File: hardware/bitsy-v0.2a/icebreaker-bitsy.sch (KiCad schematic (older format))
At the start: 94 parts, among them J1 Conn_01x01, J10 Conn_01x01, J11 Conn_01x01, J12 Conn_01x01, J13 Conn_01x01, J14 Jumper, J15 Jumper, J16 Jumper, J17 Jumper, J18 Jumper, J19 Jumper, J2 Conn_01x01, J20 Conn_01x01, J21 Conn_01x01, J22 Conn_01x01, J23 Conn_01x01, J24 Conn_01x01, J25 Conn_01x01, J26 Conn_01x01, J27 Conn_01x01, J28 Conn_01x01, J29 Conn_01x01, J3 Conn_01x01, J30 Conn_01x01, J31 Conn_01x01, J32 Conn_01x01, J33 Conn_01x01, J34 Conn_01x01, J35 Conn_01x01, J36 Conn_01x01, J37 Conn_01x01, J38 Jumper, J4 Conn_01x01, J41 Conn_01x01, J42 Conn_01x01, J43 Conn_01x01, J44 Conn_01x01, J45 Conn_01x01, J46 Conn_01x01, J47 Conn_01x01, J48 Conn_01x01, J49 Conn_01x01, J5 Conn_01x01, J6 Conn_01x01, J7 Conn_01x01, J8 Conn_01x01, J9 Conn_01x01, P1 USB_OTG, SW1 TACT, U1 USBLC6-2, U2 3.3V, U3 1V2, U5 W25Q, U6 ICE5LP4K-SG48, X1 12MHz

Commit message: Fixed #6 Oscillator pinout and schematic symbol.
Both bitsy and icebreaker.
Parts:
- X1: symbol pkl_device:Oscillator -> pkl_device:pkl_oscillator_sit2001
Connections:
- wire segments 315 -> 311
- no-connect marks 1 -> 2
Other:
- moved on the sheet: C4, R7
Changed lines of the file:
@@
 Title "iCEBreaker-bitsy"
 Date ""
-Rev "V0.2a"
+Rev "V0.1a"
 Comp "1BitSquared"
 Comment1 "2018 (C) 1BitSquared <info@1bitsquared.com>"
@@
 $EndComp
 $Comp
-L pkl_device:Oscillator X1
+L pkl_device:pkl_oscillator_sit2001 X1
 U 1 1 5A523EA3
-P 1550 3150
-F 0 "X1" H 1550 2755 60  0000 C CNN
-F 1 "12MHz" H 1550 2865 60  0000 C CNN
-F 2 "pkl_housings_sot:SOT-23-5" H 1550 3150 60  0001 C CNN
-F 3 "https://www.sitime.com/datasheet/SiT2001" H 1550 3150 60  0001 C CNN
-F 4 "12MHz Oscillator" H 1550 3150 50  0001 C CNN "Description"
-F 5 "SiTIME" H 1550 3150 50  0001 C CNN "Manufacturer"
-F 6 "SIT2001BI-S2-33E-12.000000G" H 1550 3150 50  0001 C CNN "MFN"
-F 7 "ANY" H 1550 3150 50  0001 C CNN "Source"
-F 8 "xtal-sot23-5-12mhz-osc" H -350 -3600 50  0001 C CNN "Key"
-	1    1550 3150
-	-1   0    0    1
+P 1750 3250
+F 0 "X1" H 1750 3600 60  0000 C CNN
+F 1 "12MHz" H 1750 3500 60  0000 C CNN
+F 2 "pkl_housings_sot:SOT-23-5" H 1750 3250 60  0001 C CNN
+F 3 "https://www.sitime.com/datasheet/SiT2001" H 1750 3250 60  0001 C CNN
+F 4 "xtal-sot23-5-12mhz-osc" H -150 -3500 50  0001 C CNN "Key"
+F 5 "12MHz Oscillator" H 1750 3250 50  0001 C CNN "Description"
+F 6 "SiTIME" H 1750 3250 50  0001 C CNN "Manufacturer"
+F 7 "SIT2001BI-S2-33E-12.000000G" H 1750 3250 50  0001 C CNN "MFN"
+F 8 "ANY" H 1750 3250 50  0001 C CNN "Source"
+	1    1750 3250
+	-1   0    0    -1
 $EndComp
 $Comp
 L pkl_device:pkl_R_Small R7
 U 1 1 5A52417F
-P 2150 3150
-F 0 "R7" V 2200 3300 50  0000 C CNN
-F 1 "10k" V 2200 3000 50  0000 C CNN
-F 2 "pkl_dipol:R_0402" H 2209 3057 60  0001 L CNN
-F 3 "" H 2150 3150 60  0000 C CNN
-F 4 "ANY" H 2150 3150 50  0001 C CNN "Source"
-F 5 "res-0402-10k" H -350 -3600 50  0001 C CNN "Key"
-	1    2150 3150
-	0    1    1    0
+P 1050 3150
+F 0 "R7" V 1100 3300 50  0000 C CNN
+F 1 "10k" V 1100 3000 50  0000 C CNN
+F 2 "pkl_dipol:R_0402" H 1109 3057 60  0001 L CNN
+F 3 "" H 1050 3150 60  0000 C CNN
+F 4 "ANY" H 1050 3150 50  0001 C CNN "Source"
+F 5 "res-0402-10k" H -1450 -3600 50  0001 C CNN "Key"
+	1    1050 3150
+	0    -1   -1   0
 $EndComp
 $Comp
 L power:+3V3 #PWR02
 U 1 1 5A524395
-P 2450 2950
-F 0 "#PWR02" H 2450 2800 50  0001 C CNN
-F 1 "+3V3" H 2465 3126 50  0000 C CNN
-F 2 "" H 2450 2950 50  0001 C CNN
-F 3 "" H 2450 2950 50  0001 C CNN
-	1    2450 2950
+P 2350 3050
+F 0 "#PWR02" H 2350 2900 50  0001 C CNN
+F 1 "+3V3" H 2365 3226 50  0000 C CNN
+F 2 "" H 2350 3050 50  0001 C CNN
+F 3 "" H 2350 3050 50  0001 C CNN
+	1    2350 3050
 	1    0    0    -1
 $EndComp
@@
 L power:+3V3 #PWR03
 U 1 1 5A5243FF
-P 1050 2950
-F 0 "#PWR03" H 1050 2800 50  0001 C CNN
-F 1 "+3V3" H 1065 3126 50  0000 C CNN
-F 2 "" H 1050 2950 50  0001 C CNN
-F 3 "" H 1050 2950 50  0001 C CNN
-	1    1050 2950
+P 850 3050
+F 0 "#PWR03" H 850 2900 50  0001 C CNN
+F 1 "+3V3" H 865 3226 50  0000 C CNN
+F 2 "" H 850 3050 50  0001 C CNN
+F 3 "" H 850 3050 50  0001 C CNN
+	1    850  3050
 	1    0    0    -1
 $EndComp
@@
 L pkl_device:pkl_C_Small C4
 U 1 1 5A526171
-P 850 3250
-F 0 "C4" H 942 3297 50  0000 L CNN
-F 1 "100n" H 942 3204 50  0000 L CNN
-F 2 "pkl_dipol:C_0402" H 942 3157 60  0001 L CNN
-F 3 "" H 850 3250 60  0000 C CNN
-F 4 "ANY" H 850 3250 50  0001 C CNN "Source"
-F 5 "cap-cer-0402-100n" H -350 -3600 50  0001 C CNN "Key"
-	1    850  3250
-	-1   0    0    -1
+P 2350 3550
+F 0 "C4" H 2442 3597 50  0000 L CNN
+F 1 "100n" H 2442 3504 50  0000 L CNN
+F 2 "pkl_dipol:C_0402" H 2442 3457 60  0001 L CNN
+F 3 "" H 2350 3550 60  0000 C CNN
+F 4 "ANY" H 2350 3550 50  0001 C CNN "Source"
+F 5 "cap-cer-0402-100n" H 1150 -3300 50  0001 C CNN "Key"
+	1    2350 3550
+	1    0    0    -1
 $EndComp
 $Comp
 L power:GND #PWR05
 U 1 1 5A52451B
-P 950 3550
-F 0 "#PWR05" H 950 3300 50  0001 C CNN
-F 1 "GND" H 955 3374 50  0000 C CNN
-F 2 "" H 950 3550 50  0001 C CNN
-F 3 "" H 950 3550 50  0001 C CNN
-	1    950  3550
-	1    0    0    -1
-$EndComp
-Text Notes 1950 3350 0    50   ~ 0
+P 1150 3750
+F 0 "#PWR05" H 1150 3500 50  0001 C CNN
+F 1 "GND" H 1155 3574 50  0000 C CNN
+F 2 "" H 1150 3750 50  0001 C CNN
+F 3 "" H 1150 3750 50  0001 C CNN
+	1    1150 3750
+	1    0    0    -1
+$EndComp
+Text Notes 650  3300 0    50   ~ 0
 10k or less
 $Comp
@@
 Text Label 9300 4100 0    50   ~ 0
 FLASH_~HLD~/~RST~/IO3
-Text Label 2050 3050 0    50   ~ 0
+Text Label 2450 3350 0    50   ~ 0
 CLK
 Text Label 9400 2400 0    50   ~ 0
@@
 	4700 5700 4700 7700
 Wire Wire Line
-	1950 3050 2050 3050
-Wire Wire Line
-	1050 3050 1050 2950
-Wire Wire Line
-	850  3150 850  3050
-Wire Wire Line
-	850  3050 1050 3050
-Connection ~ 1050 3050
-Wire Wire Line
-	1150 3050 1050 3050
-Wire Wire Line
-	1150 3150 1050 3150
-Wire Wire Line
-	850  3350 850  3450
-Wire Wire Line
-	950  3450 950  3550
-Wire Wire Line
-	850  3450 950  3450
-Connection ~ 950  3450
-Wire Wire Line
-	950  3450 1050 3450
-Wire Wire Line
-	1050 3150 1050 3450
-Wire Wire Line
-	2250 3150 2450 3150
-Wire Wire Line
-	2450 2950 2450 3150
-Wire Wire Line
-	1950 3150 2050 3150
+	2250 3350 2450 3350
+Wire Wire Line
+	2250 3150 2350 3150
+Wire Wire Line
+	2350 3150 2350 3050
+Wire Wire Line
+	2350 3150 2350 3450
+Connection ~ 2350 3150
+Wire Wire Line
+	2350 3650 2350 3750
+$Comp
+L power:GND #PWR?
+U 1 1 5B81576B
+P 2350 3750
+F 0 "#PWR?" H 2350 3500 50  0001 C CNN
+F 1 "GND" H 2355 3574 50  0000 C CNN
+F 2 "" H 2350 3750 50  0001 C CNN
+F 3 "" H 2350 3750 50  0001 C CNN
+	1    2350 3750
+	1    0    0    -1
+$EndComp
+Wire Wire Line
+	1250 3350 1150 3350
+Wire Wire Line
+	1150 3350 1150 3750
+Wire Wire Line
+	850  3050 850  3150
+Wire Wire Line
+	850  3150 950  3150
+Wire Wire Line
+	1150 3150 1250 3150
+NoConn ~ 1250 3250
 $EndSCHEMATC

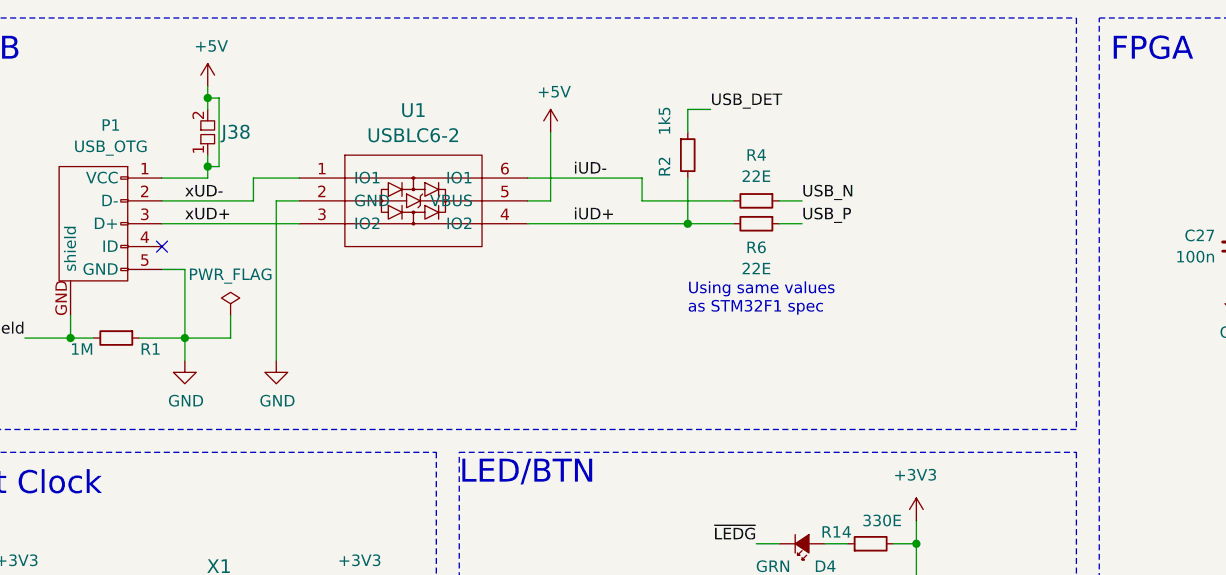
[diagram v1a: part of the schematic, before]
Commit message: Added USB pads for easier debugging and hardwired USB connection.
This patch fixes #8
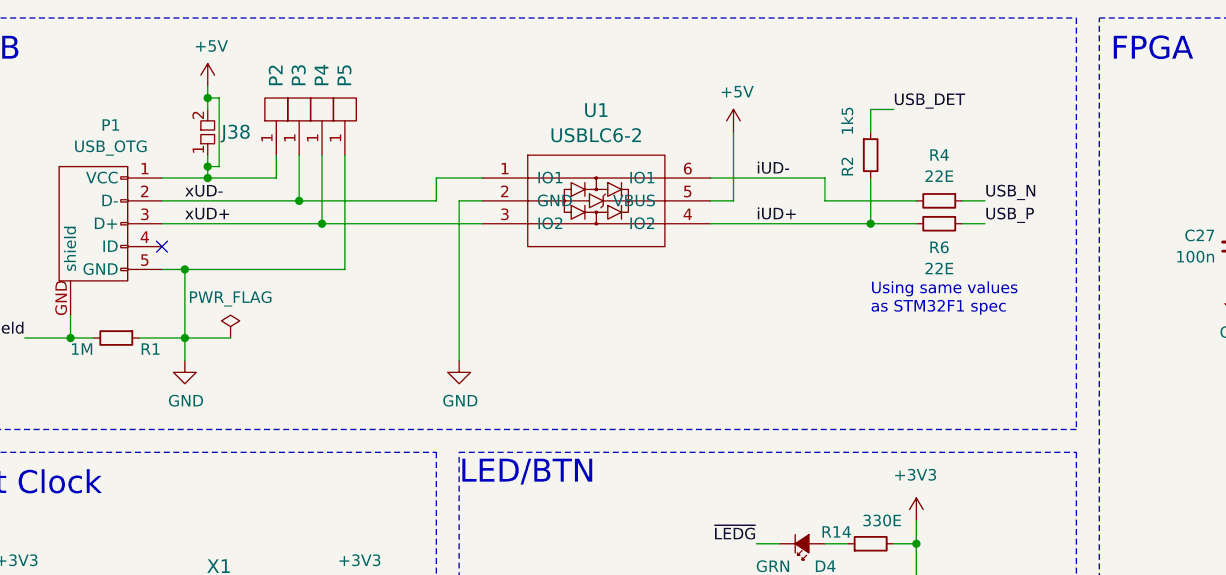
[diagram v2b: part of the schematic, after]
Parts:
- added P2, P3, P4, P5: UP, pkl_pads:PAD_SMD_1x2.65, symbol pkl_misc:PAD_SMD
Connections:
- net +5V: now also P2.1 (PAD)
- net GND: now also P5.1 (PAD)
- net xUD+: now also P4.1 (PAD)
- net xUD-: now also P3.1 (PAD)
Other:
- moved on the sheet: R2, R4, R6, U1
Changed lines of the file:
@@
 L power:PWR_FLAG #FLG01
 U 1 1 5A530EEE
-P 1800 1800
-F 0 "#FLG01" H 1800 1875 50  0001 C CNN
-F 1 "PWR_FLAG" H 1800 1977 50  0000 C CNN
-F 2 "" H 1800 1800 50  0001 C CNN
-F 3 "" H 1800 1800 50  0001 C CNN
-	1    1800 1800
+P 1800 1900
+F 0 "#FLG01" H 1800 1975 50  0001 C CNN
+F 1 "PWR_FLAG" H 1800 2077 50  0000 C CNN
+F 2 "" H 1800 1900 50  0001 C CNN
+F 3 "" H 1800 1900 50  0001 C CNN
+	1    1800 1900
 	1    0    0    -1
 $EndComp
 Wire Wire Line
 	1600 1900 1800 1900
-Wire Wire Line
-	1800 1900 1800 1800
 Wire Wire Line
 	1500 1200 1700 1200
@@
 L pkl_device:pkl_R_Small R2
 U 1 1 5AAF697C
-P 3800 1100
-F 0 "R2" V 3700 1050 50  0000 C CNN
-F 1 "1k5" V 3700 1250 50  0000 C CNN
-F 2 "pkl_dipol:R_0402" H 3859 1007 60  0001 L CNN
-F 3 "" H 3800 1100 60  0000 C CNN
-F 4 "res-0402-1k5" H -7400 -4300 50  0001 C CNN "Key"
-F 5 "ANY" H 3800 1100 50  0001 C CNN "Source"
-	1    3800 1100
-	1    0    0    -1
-$EndComp
-Wire Wire Line
-	3800 1400 3800 1200
-Wire Wire Line
-	3800 1000 3800 900
-Wire Wire Line
-	3800 900  3900 900
-Wire Wire Line
-	3800 1400 4000 1400
-Connection ~ 3800 1400
-Text Label 3900 900  0    50   ~ 0
+P 4600 1100
+F 0 "R2" V 4500 1050 50  0000 C CNN
+F 1 "1k5" V 4500 1250 50  0000 C CNN
+F 2 "pkl_dipol:R_0402" H 4659 1007 60  0001 L CNN
+F 3 "" H 4600 1100 60  0000 C CNN
+F 4 "res-0402-1k5" H -6600 -4300 50  0001 C CNN "Key"
+F 5 "ANY" H 4600 1100 50  0001 C CNN "Source"
+	1    4600 1100
+	1    0    0    -1
+$EndComp
+Wire Wire Line
+	4600 1400 4600 1200
+Wire Wire Line
+	4600 1000 4600 900
+Wire Wire Line
+	4600 900  4700 900
+Wire Wire Line
+	4600 1400 4800 1400
+Connection ~ 4600 1400
+Text Label 4700 900  0    50   ~ 0
 USB_DET
 Text Label 1600 1300 0    50   ~ 0
@@
 L pkl_device:pkl_R_Small R4
 U 1 1 5ABF926C
-P 4100 1300
-F 0 "R4" V 3901 1300 50  0000 C CNN
-F 1 "22E" V 3994 1300 50  0000 C CNN
-F 2 "pkl_dipol:R_0402" H 4159 1207 60  0001 L CNN
-F 3 "" H 4100 1300 60  0000 C CNN
-F 4 "res-0402-22" H -7100 -4100 50  0001 C CNN "Key"
-F 5 "ANY" H 4100 1300 50  0001 C CNN "Source"
-	1    4100 1300
+P 4900 1300
+F 0 "R4" V 4701 1300 50  0000 C CNN
+F 1 "22E" V 4794 1300 50  0000 C CNN
+F 2 "pkl_dipol:R_0402" H 4959 1207 60  0001 L CNN
+F 3 "" H 4900 1300 60  0000 C CNN
+F 4 "res-0402-22" H -6300 -4100 50  0001 C CNN "Key"
+F 5 "ANY" H 4900 1300 50  0001 C CNN "Source"
+	1    4900 1300
 	0    1    1    0
 $EndComp
@@
 L pkl_device:pkl_R_Small R6
 U 1 1 5ABF954F
-P 4100 1400
-F 0 "R6" V 4205 1400 50  0000 C CNN
-F 1 "22E" V 4298 1400 50  0000 C CNN
-F 2 "pkl_dipol:R_0402" H 4159 1307 60  0001 L CNN
-F 3 "" H 4100 1400 60  0000 C CNN
-F 4 "res-0402-22" H -7100 -4000 50  0001 C CNN "Key"
-F 5 "ANY" H 4100 1400 50  0001 C CNN "Source"
-	1    4100 1400
+P 4900 1400
+F 0 "R6" V 5005 1400 50  0000 C CNN
+F 1 "22E" V 5098 1400 50  0000 C CNN
+F 2 "pkl_dipol:R_0402" H 4959 1307 60  0001 L CNN
+F 3 "" H 4900 1400 60  0000 C CNN
+F 4 "res-0402-22" H -6300 -4000 50  0001 C CNN "Key"
+F 5 "ANY" H 4900 1400 50  0001 C CNN "Source"
+	1    4900 1400
 	0    1    1    0
 $EndComp
-Text Notes 3800 1800 0    50   ~ 0
+Text Notes 4600 1800 0    50   ~ 0
 Using same values\nas STM32F1 spec
 Wire Wire Line
-	4200 1300 4300 1300
-Wire Wire Line
-	4200 1400 4300 1400
-Text Label 4300 1300 0    50   ~ 0
+	5000 1300 5100 1300
+Wire Wire Line
+	5000 1400 5100 1400
+Text Label 5100 1300 0    50   ~ 0
 USB_N
-Text Label 4300 1400 0    50   ~ 0
+Text Label 5100 1400 0    50   ~ 0
 USB_P
 $Comp
@@
 L pkl_misc:USBLC6-2 U1
 U 1 1 5B3AE142
-P 2600 1300
-F 0 "U1" H 2600 1695 60  0000 C CNN
-F 1 "USBLC6-2" H 2600 1585 60  0000 C CNN
-F 2 "pkl_housings_sot:SOT-666" H 2600 1585 60  0001 C CNN
-F 3 "" H 2600 1300 60  0000 C CNN
-F 4 "tvs-diode-sot666" H 2600 1300 50  0001 C CNN "Key"
-F 5 "ANY" H 2600 1300 50  0001 C CNN "Source"
-	1    2600 1300
-	1    0    0    -1
-$EndComp
-Wire Wire Line
-	1500 1400 2100 1400
-Wire Wire Line
-	1500 1300 1900 1300
-Wire Wire Line
-	1900 1300 1900 1200
-Wire Wire Line
-	1900 1200 2100 1200
-Wire Wire Line
-	2100 1300 2000 1300
-Wire Wire Line
-	2000 1300 2000 2000
+P 3400 1300
+F 0 "U1" H 3400 1695 60  0000 C CNN
+F 1 "USBLC6-2" H 3400 1585 60  0000 C CNN
+F 2 "pkl_housings_sot:SOT-666" H 3400 1585 60  0001 C CNN
+F 3 "" H 3400 1300 60  0000 C CNN
+F 4 "tvs-diode-sot666" H 3400 1300 50  0001 C CNN "Key"
+F 5 "ANY" H 3400 1300 50  0001 C CNN "Source"
+	1    3400 1300
+	1    0    0    -1
+$EndComp
+Wire Wire Line
+	1500 1400 2200 1400
+Wire Wire Line
+	1500 1300 2100 1300
+Wire Wire Line
+	2700 1300 2700 1200
+Wire Wire Line
+	2700 1200 2900 1200
+Wire Wire Line
+	2900 1300 2800 1300
+Wire Wire Line
+	2800 1300 2800 2000
 $Comp
 L power:GND #PWR011
 U 1 1 5B505F45
-P 2000 2000
-F 0 "#PWR011" H 2000 1750 50  0001 C CNN
-F 1 "GND" H 2005 1824 50  0000 C CNN
-F 2 "" H 2000 2000 50  0001 C CNN
-F 3 "" H 2000 2000 50  0001 C CNN
-	1    2000 2000
-	1    0    0    -1
-$EndComp
-Text Label 3300 1200 0    50   ~ 0
+P 2800 2000
+F 0 "#PWR011" H 2800 1750 50  0001 C CNN
+F 1 "GND" H 2805 1824 50  0000 C CNN
+F 2 "" H 2800 2000 50  0001 C CNN
+F 3 "" H 2800 2000 50  0001 C CNN
+	1    2800 2000
+	1    0    0    -1
+$EndComp
+Text Label 4100 1200 0    50   ~ 0
 iUD-
-Text Label 3300 1400 0    50   ~ 0
+Text Label 4100 1400 0    50   ~ 0
 iUD+
 Wire Wire Line
-	3100 1200 3600 1200
-Wire Wire Line
-	3600 1200 3600 1300
-Wire Wire Line
-	3600 1300 4000 1300
-Wire Wire Line
-	3100 1400 3800 1400
-Wire Wire Line
-	3100 1300 3200 1300
-Wire Wire Line
-	3200 1300 3200 1000
+	3900 1200 4400 1200
+Wire Wire Line
+	4400 1200 4400 1300
+Wire Wire Line
+	4400 1300 4800 1300
+Wire Wire Line
+	3900 1400 4600 1400
+Wire Wire Line
+	3900 1300 4000 1300
+Wire Wire Line
+	4000 1300 4000 1000
 $Comp
 L power:+5V #PWR012
 U 1 1 5B5C49E6
-P 3200 1000
-F 0 "#PWR012" H 3200 850 50  0001 C CNN
-F 1 "+5V" H 3215 1176 50  0000 C CNN
-F 2 "" H 3200 1000 50  0001 C CNN
-F 3 "" H 3200 1000 50  0001 C CNN
-	1    3200 1000
+P 4000 1000
+F 0 "#PWR012" H 4000 850 50  0001 C CNN
+F 1 "+5V" H 4015 1176 50  0000 C CNN
+F 2 "" H 4000 1000 50  0001 C CNN
+F 3 "" H 4000 1000 50  0001 C CNN
+	1    4000 1000
 	1    0    0    -1
 $EndComp
@@
 	2350 3650 2350 3750
 $Comp
-L power:GND #PWR?
+L power:GND #PWR0101
 U 1 1 5B81576B
 P 2350 3750
-F 0 "#PWR?" H 2350 3500 50  0001 C CNN
+F 0 "#PWR0101" H 2350 3500 50  0001 C CNN
 F 1 "GND" H 2355 3574 50  0000 C CNN
 F 2 "" H 2350 3750 50  0001 C CNN
@@
 	1150 3150 1250 3150
 NoConn ~ 1250 3250
+$Comp
+L pkl_misc:PAD_SMD P2
+U 1 1 5D65C8E0
+P 2000 900
+F 0 "P2" H 2200 900 60  0000 R CNN
+F 1 "UP" V 2200 950 60  0001 R CNN
+F 2 "pkl_pads:PAD_SMD_1x2.65" H 2000 650 60  0001 C CNN
+F 3 "" H 2000 750 60  0000 C CNN
+F 4 "ANY" H 2000 900 50  0001 C CNN "Source"
+	1    2000 900
+	0    -1   -1   0
+$EndComp
+$Comp
+L pkl_misc:PAD_SMD P3
+U 1 1 5D65D33D
+P 2100 900
+F 0 "P3" H 2300 900 60  0000 R CNN
+F 1 "UP" V 2300 950 60  0001 R CNN
+F 2 "pkl_pads:PAD_SMD_1x2.65" H 2100 650 60  0001 C CNN
+F 3 "" H 2100 750 60  0000 C CNN
+F 4 "ANY" H 2100 900 50  0001 C CNN "Source"
+	1    2100 900
+	0    -1   -1   0
+$EndComp
+$Comp
+L pkl_misc:PAD_SMD P4
+U 1 1 5D65D419
+P 2200 900
+F 0 "P4" H 2400 900 60  0000 R CNN
+F 1 "UP" V 2400 950 60  0001 R CNN
+F 2 "pkl_pads:PAD_SMD_1x2.65" H 2200 650 60  0001 C CNN
+F 3 "" H 2200 750 60  0000 C CNN
+F 4 "ANY" H 2200 900 50  0001 C CNN "Source"
+	1    2200 900
+	0    -1   -1   0
+$EndComp
+$Comp
+L pkl_misc:PAD_SMD P5
+U 1 1 5D65D4F7
+P 2300 900
+F 0 "P5" H 2500 900 60  0000 R CNN
+F 1 "UP" V 2500 950 60  0001 R CNN
+F 2 "pkl_pads:PAD_SMD_1x2.65" H 2300 650 60  0001 C CNN
+F 3 "" H 2300 750 60  0000 C CNN
+F 4 "ANY" H 2300 900 50  0001 C CNN "Source"
+	1    2300 900
+	0    -1   -1   0
+$EndComp
+Wire Wire Line
+	2000 1100 2000 1200
+Wire Wire Line
+	2000 1200 1700 1200
+Connection ~ 1700 1200
+Wire Wire Line
+	2100 1100 2100 1300
+Connection ~ 2100 1300
+Wire Wire Line
+	2100 1300 2700 1300
+Wire Wire Line
+	2200 1100 2200 1400
+Connection ~ 2200 1400
+Wire Wire Line
+	2200 1400 2900 1400
+Wire Wire Line
+	2300 1100 2300 1600
+Wire Wire Line
+	2300 1600 1600 1600
+Connection ~ 1600 1600
 $EndSCHEMATC
